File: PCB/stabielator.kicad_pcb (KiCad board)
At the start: 4 copper layers, 50 x 50 mm, 104 parts, among them J1 S2B-PH, J2 SH_SM02B, J3 SH_SM02B, J4 SH_SM02B, J5 USB4105-GF-A, J6 SH_SM02B, Q1 2N7002, SW1 BOOT, SW2 PWR, U1 ESP32-C3-MINI-1, U10 DRV2605LDGS, U11 TPS3424A11C13ADRLR, U2 DRV2605LDGS, U3 BQ24074RGT, U4 TPS63001, U5 DRV2605LDGS, U6 DRV2605LDGS, U7 BNO086, U8 TCA9546APW, U9 USBLC6-2SC6

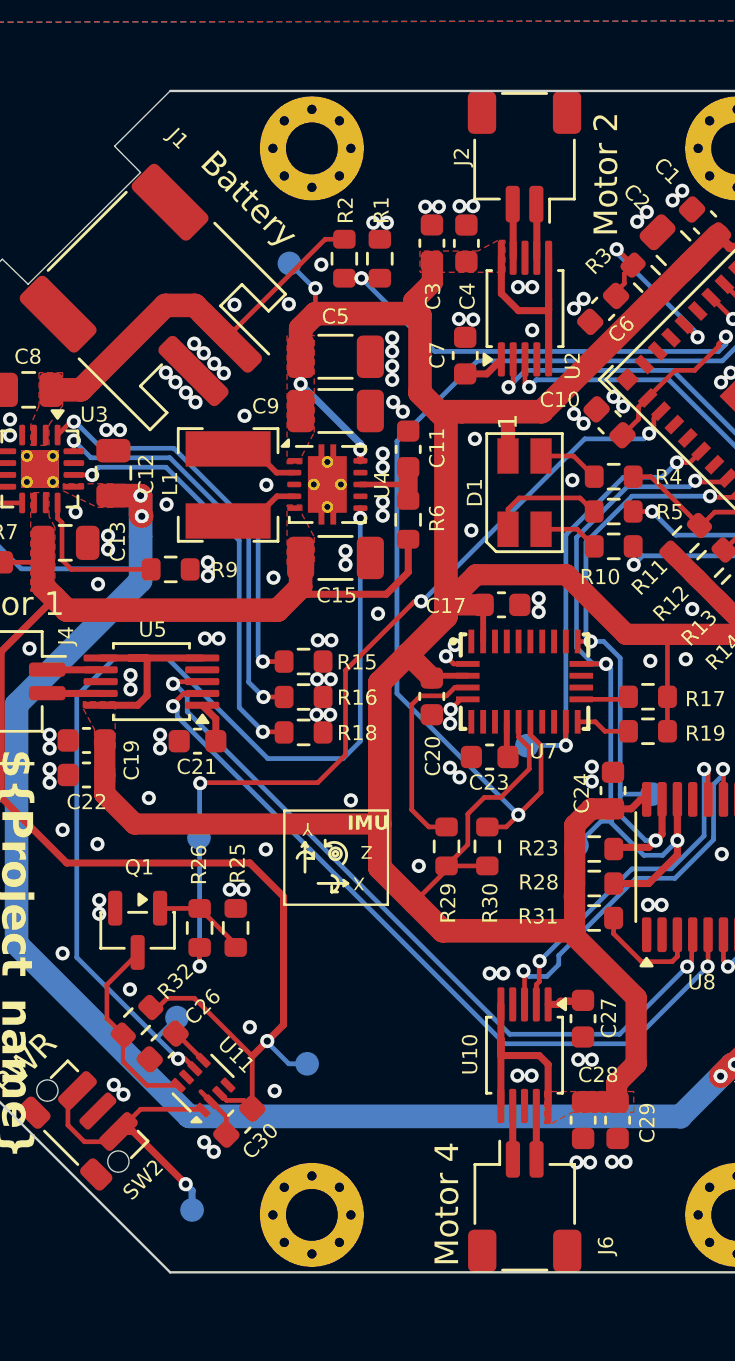
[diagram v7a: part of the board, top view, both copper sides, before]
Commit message: Feedback Elect
- Thermal reliefs toegepast op een aantal extra onderdelen
- U7 (LGA-28) footprint pads + pasta/masker aangepast (80% pasta dekking aangeraden door fabrikant)
- Algemene soldeer masker expansie op 0 gezet
- 2x 0.5mm fiducial toegevoegd
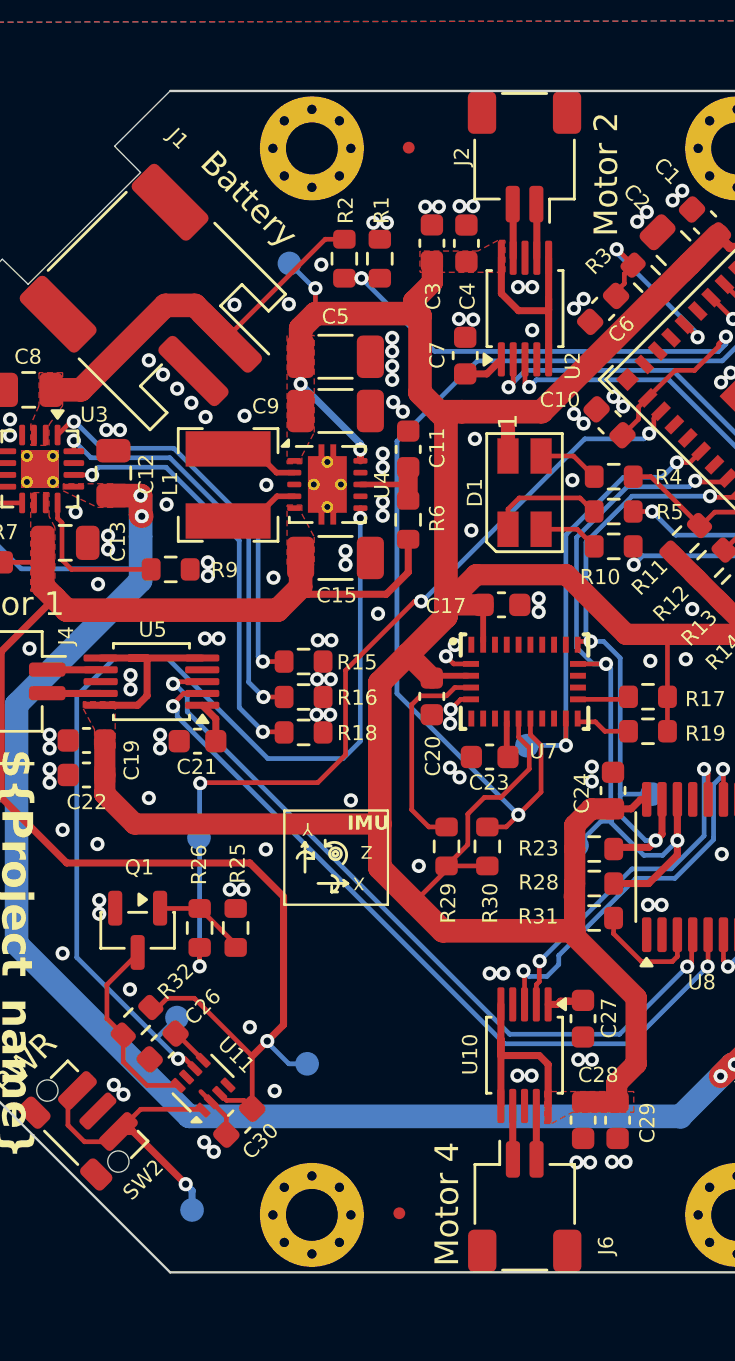
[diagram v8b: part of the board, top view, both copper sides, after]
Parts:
- added FID1: Fiducial, Fiducial:Fiducial_0.5mm_Mask1mm, F.Cu at (120.1, 52.4)
- added FID2: Fiducial, Fiducial:Fiducial_0.5mm_Mask1mm, F.Cu at (119.7, 97.5)
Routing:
- net GND: vias 189 -> 186
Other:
- rule pad_to_mask_clearance: 0.05 -> 0
